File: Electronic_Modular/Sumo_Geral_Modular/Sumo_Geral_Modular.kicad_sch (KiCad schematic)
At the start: 26 parts, among them J1 Conn_01x02, J10 Conn_01x03, J11 Conn_01x03, J2 Conn_01x05, J3 Conn_01x05, J4 Conn_01x05, J5 Conn_01x03, J6 Conn_01x08, J7 Conn_01x08, J8 Conn_01x02, J9 Conn_01x02, SW1 SW_Push, SW2 SW_Push, SW3 SW_Push, U1 AMS1117-5.0, U2 AMS1117-3.3

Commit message: chore: continue development modular pcb
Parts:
- added C7: 100uF, symbol Device:C
- added D2: D, symbol Device:D
- added J12: USB_B_Micro, symbol Connector:USB_B_Micro
- added Q1, Q2: S8050, Package_TO_SOT_THT:TO-92_Inline, symbol Transistor_BJT:S8050
- added R4, R5: 1K, symbol Device:R
- added R6, R7: 10K, symbol Device:R
- added U3: CH340C, Package_SO:SOIC-16_3.9x9.9mm_P1.27mm, symbol Interface_USB:CH340C
- added U4: ESP32-WROOM-32UE, RF_Module:ESP32-WROOM-32UE, symbol RF_Module:ESP32-WROOM-32UE
- J6: value Conn_01x08 -> p H ld e
- J7: value Conn_01x08 -> p H ld d
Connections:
- net 3V3: now also R1.2, R2.2, C7.1, U3.16 (VCC), U3.4 (V3), U4.2 (VDD)
- net 5V: now also D2.1 (K)
- net EN: now also Q1.3 (C), U4.3 (EN)
- net GND: now also C1.2, C2.2, C3.2, C4.2, J1.2 (Pin_2), R3.2, U1.1 (GND), U2.1 (GND), C7.2, J12.5 (GND), J12.6 (Shield), U3.1 (GND), U4.1 (GND), U4.15 (GND), U4.38 (GND), U4.39 (GND); no longer R1.2, R2.2
- net SCL: now also R1.1, U4.36 (IO22); no longer R2.1
- net SDA: now also R2.1, U4.33 (IO21); no longer R1.1
- new net: R5.2, U3.3 (RXD)
- new net: Q2.1 (E), R7.2, U3.14 (~{RTS})
- new net: Q2.2 (B), R7.1
- new net: D2.2 (A), J12.1 (VBUS)
- new net: J12.2 (D-), U3.6 (UD-)
- new net: J12.3 (D+), U3.5 (UD+)
- new net: Q1.1 (E), R6.2, U3.13 (~{DTR})
- new net: Q1.2 (B), R6.1
- new net: R4.2, U3.2 (TXD)
- new net I00: Q2.3 (C)
- new net IO0: U4.25 (IO0)
- new net RXD0: R5.1
- new net TXD0: R4.1
- no-connect marks 5 -> 14
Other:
- moved on the sheet: C1, C2, C3, C4, C5, C6, D1, J1, J10, J11, J2, J3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

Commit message: chore: finish the schematic and set footprints
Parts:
- added D3: LED, symbol Device:LED
- added J13: SENSOR DE MOUSE, Connector_JST:JST_XH_S5B-XH-A_1x05_P2.50mm_Horizontal, symbol Connector_Generic:Conn_01x05
- added J14: ALIMENTAÇÃO SDM, Connector_JST:JST_XH_S2B-XH-A_1x02_P2.50mm_Horizontal, symbol Connector_Generic:Conn_01x02
- added J15: MPU, Connector_PinSocket_2.54mm:PinSocket_1x08_P2.54mm_Vertical, symbol Connector_Generic:Conn_01x08
- added R8: 330, symbol Device:R
- J2: value Conn_01x05 -> VL53L0X 1; footprint (none) -> Connector_JST:JST_XH_B5B-XH-AM_1x05_P2.50mm_Vertical
- J3: value Conn_01x05 -> VL53L0X 2; footprint (none) -> Connector_JST:JST_XH_B5B-XH-AM_1x05_P2.50mm_Vertical
- J4: value Conn_01x05 -> VL53L0X 3; footprint (none) -> Connector_JST:JST_XH_B5B-XH-AM_1x05_P2.50mm_Vertical
- J5: value Conn_01x03 -> VS1838B; footprint (none) -> Connector_PinHeader_2.54mm:PinHeader_1x03_P2.54mm_Vertical
- J6: value p H ld e -> ponte H ld e; footprint (none) -> Connector_PinSocket_2.54mm:PinSocket_1x08_P2.54mm_Vertical
- J7: value p H ld d -> ponte H ld d; footprint (none) -> Connector_PinSocket_2.54mm:PinSocket_1x08_P2.54mm_Vertical
- J8, J9: footprint (none) -> Connector_PinSocket_2.54mm:PinSocket_1x02_P2.54mm_Vertical
- R3: value R -> 1K
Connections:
- net STBY is gone; now on net 3V3: J7.4 (Pin_4)
- net 2s: now also R3.1; no longer D1.2 (A)
- net 3V3: now also J14.1 (Pin_1), J15.1 (Pin_1)
- net AIN1: now also U4.9 (IO33)
- net AIN2: now also U4.10 (IO25)
- net BIN1: now also U4.13 (IO14)
- net BIN2: now also U4.14 (IO12)
- net ESC 1: now also U4.28 (IO17)
- net ESC 2: now also U4.27 (IO16)
- net GND: now also D1.1 (K), D3.1 (K), J14.2 (Pin_2), J15.2 (Pin_2), J15.7 (Pin_7); no longer R3.2
- net IR: now also U4.8 (IO32)
- net RXD0: now also U4.34 (RXD0/IO3)
- net SCL: now also J15.3 (Pin_3)
- net SDA: now also J15.4 (Pin_4)
- net TXD0: now also U4.35 (TXD0/IO1)
- net XSH1: now also U4.6 (IO34)
- net XSH2: now also U4.7 (IO35)
- net XSH3: now also U4.12 (IO27)
- net MOTION: now reaches U4.11 (IO26)
- net MOTION: now also J13.5 (Pin_5)
- net SS/CS: now reaches U4.23 (IO15)
- net SS/CS: now also J13.1 (Pin_1)
- net at U4.24 (IO2): now also R8.1
- net SCLK: now reaches U4.30 (IO18)
- net SCLK: now also J13.3 (Pin_3)
- net MISO: now reaches U4.31 (IO19)
- net MISO: now also J13.2 (Pin_2)
- net MOSI: now reaches U4.37 (IO23)
- net MOSI: now also J13.4 (Pin_4)
- new net: D3.2 (A), R8.2
- new net: D1.2 (A), R3.2
- new net INT: J15.8 (Pin_8)
- no-connect marks 14 -> 18
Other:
- moved on the sheet: C5, C6, C7, D1, D2, J10, J11, J12, J2, J3, J4, J5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

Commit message: chore: set all footprints
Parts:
- C1, C2, C3, C4, C5, C6, C7: footprint (none) -> Capacitor_SMD:C_0201_0603Metric
- D1, D3: footprint (none) -> LED_SMD:LED_0201_0603Metric
- D2: footprint (none) -> Diode_SMD:D_0201_0603Metric
- J1: footprint (none) -> Connector_JST:JST_PH_B2B-PH-K_1x02_P2.00mm_Vertical
- J10, J11: footprint (none) -> Connector_JST:JST_XH_B3B-XH-A_1x03_P2.50mm_Vertical
- J12: footprint (none) -> Connector_USB:USB_Micro-B_Amphenol_10118194_Horizontal
- R1, R2, R3, R4, R5, R6, R7, R8: footprint (none) -> Resistor_SMD:R_0201_0603Metric
- SW1: footprint (none) -> Button_Switch_THT:Nidec_Copal_SH-7010C
- SW2, SW3: footprint (none) -> Button_Switch_SMD:SW_SPST_TL3342
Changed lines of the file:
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@@
 			)
 		)
-		(property "Footprint" ""
+		(property "Footprint" "Connector_JST:JST_PH_B2B-PH-K_1x02_P2.00mm_Vertical"
 			(at 30.48 167.64 0)
 			(effects
@@
 			)
 		)
-		(property "Footprint" ""
+		(property "Footprint" "Capacitor_SMD:C_0201_0603Metric"
 			(at 83.5152 182.88 0)
 			(effects
@@
 			)
 		)
-		(property "Footprint" ""
+		(property "Footprint" "Resistor_SMD:R_0201_0603Metric"
 			(at 206.502 49.53 90)
 			(effects
@@
 			)
 		)
-		(property "Footprint" ""
+		(property "Footprint" "Capacitor_SMD:C_0201_0603Metric"
 			(at 124.1552 182.88 0)
 			(effects
@@
 			)
 		)
-		(property "Footprint" ""
+		(property "Footprint" "Resistor_SMD:R_0201_0603Metric"
 			(at 242.57 130.302 90)
 			(effects
@@
 			)
 		)
-		(property "Footprint" ""
+		(property "Footprint" "Capacitor_SMD:C_0201_0603Metric"
 			(at 96.2152 182.88 0)
 			(effects
@@
 			)
 		)
-		(property "Footprint" ""
+		(property "Footprint" "Capacitor_SMD:C_0201_0603Metric"
 			(at 199.0852 120.65 0)
 			(effects
@@
 			)
 		)
-		(property "Footprint" ""
+		(property "Footprint" "Resistor_SMD:R_0201_0603Metric"
 			(at 176.53 31.242 90)
 			(effects
@@
 			)
 		)
-		(property "Footprint" ""
+		(property "Footprint" "Button_Switch_THT:Nidec_Copal_SH-7010C"
 			(at 48.26 162.56 0)
 			(effects
@@
 			)
 		)
-		(property "Footprint" ""
+		(property "Footprint" "Resistor_SMD:R_0201_0603Metric"
 			(at 52.832 175.26 90)
 			(effects
@@
 			)
 		)
-		(property "Footprint" ""
+		(property "Footprint" "Resistor_SMD:R_0201_0603Metric"
 			(at 212.852 68.58 90)
 			(effects
@@
 			)
 		)
-		(property "Footprint" ""
+		(property "Footprint" "LED_SMD:LED_0201_0603Metric"
 			(at 54.61 184.15 0)
 			(effects
@@
 			)
 		)
-		(property "Footprint" ""
+		(property "Footprint" "Connector_USB:USB_Micro-B_Amphenol_10118194_Horizontal"
 			(at 182.88 138.43 0)
 			(effects
@@
 			)
 		)
-		(property "Footprint" ""
+		(property "Footprint" "Connector_JST:JST_XH_B3B-XH-A_1x03_P2.50mm_Vertical"
 			(at 39.37 127 0)
 			(effects
@@
 			)
 		)
-		(property "Footprint" ""
+		(property "Footprint" "Capacitor_SMD:C_0201_0603Metric"
 			(at 75.8952 73.66 0)
 			(effects
@@
 			)
 		)
-		(property "Footprint" ""
+		(property "Footprint" "Resistor_SMD:R_0201_0603Metric"
 			(at 248.92 141.732 90)
 			(effects
@@
 			)
 		)
-		(property "Footprint" ""
+		(property "Footprint" "LED_SMD:LED_0201_0603Metric"
 			(at 184.15 33.02 0)
 			(effects
@@
 			)
 		)
-		(property "Footprint" ""
+		(property "Footprint" "Diode_SMD:D_0201_0603Metric"
 			(at 193.04 132.08 0)
 			(effects
@@
 			)
 		)
-		(property "Footprint" ""
+		(property "Footprint" "Button_Switch_SMD:SW_SPST_TL3342"
 			(at 19.05 72.39 0)
 			(effects
@@
 			)
 		)
-		(property "Footprint" ""
+		(property "Footprint" "Resistor_SMD:R_0201_0603Metric"
 			(at 247.65 154.432 90)
 			(effects
@@
 			)
 		)
-		(property "Footprint" ""
+		(property "Footprint" "Capacitor_SMD:C_0201_0603Metric"
 			(at 63.1952 182.88 0)
 			(effects
@@
 			)
 		)
-		(property "Footprint" ""
+		(property "Footprint" "Button_Switch_SMD:SW_SPST_TL3342"
 			(at 57.15 72.39 0)
 			(effects
@@
 			)
 		)
-		(property "Footprint" ""
+		(property "Footprint" "Capacitor_SMD:C_0201_0603Metric"
 			(at 37.7952 73.66 0)
 			(effects
@@
 			)
 		)
-		(property "Footprint" ""
+		(property "Footprint" "Connector_JST:JST_XH_B3B-XH-A_1x03_P2.50mm_Vertical"
 			(at 39.37 140.97 0)
 			(effects
@@
 			)
 		)
-		(property "Footprint" ""
+		(property "Footprint" "Resistor_SMD:R_0201_0603Metric"
 			(at 242.57 127.762 90)
 			(effects

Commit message: shore: update PCB
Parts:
- added R9: 10K, Resistor_SMD:R_0201_0603Metric, symbol Device:R
- J1: value Conn_01x02 -> Bateria
- J10: value Conn_01x03 -> ESC1
- J11: value Conn_01x03 -> ESC2
- J8, J9: footprint Connector_PinSocket_2.54mm:PinSocket_1x02_P2.54mm_Vertical -> Connector_JST:JST_XH_B2B-XH-AM_1x02_P2.50mm_Vertical
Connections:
- net 3V3: now also R9.2; no longer C6.1, SW3.1
- net AO1: now also J8.2 (Pin_2); no longer J8.1 (Pin_1)
- net AO2: now also J8.1 (Pin_1); no longer J8.2 (Pin_2)
- net EN: now also C5.2; no longer C5.1
- net GND: now also C5.1; no longer C5.2
- net I00: now also C6.1, SW3.1, R9.1
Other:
- moved on the sheet: C5

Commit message: shore: PCB review
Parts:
- added D4: 1N4007, Diode_SMD:D_0603_1608Metric, symbol Device:D
- added D5: LED, LED_SMD:LED_0603_1608Metric, symbol Device:LED
- added R10: 10K, Capacitor_SMD:C_0603_1608Metric, symbol Device:R
- added R11, R12: 10K, Resistor_SMD:R_0603_1608Metric, symbol Device:R
- added R13: 1K, Resistor_SMD:R_0603_1608Metric, symbol Device:R
- C1, C2, C3, C4, C7: footprint Capacitor_SMD:C_0201_0603Metric -> Capacitor_SMD:C_0603_1608Metric
- C5, C6: value 10uF -> 100nF; footprint Capacitor_SMD:C_0201_0603Metric -> Capacitor_SMD:C_0603_1608Metric
- D1, D3: footprint LED_SMD:LED_0201_0603Metric -> LED_SMD:LED_0603_1608Metric
- D2: value D -> 1N4007; footprint Diode_SMD:D_0201_0603Metric -> Diode_SMD:D_0603_1608Metric
- J13: value SENSOR DE MOUSE -> ADSN-9500
- J14: value ALIMENTAÇÃO SDM -> PS ADSN-9500
- J15: value MPU -> MPU-6050
- J5: footprint Connector_PinHeader_2.54mm:PinHeader_1x03_P2.54mm_Vertical -> Connector_PinHeader_2.00mm:PinHeader_1x03_P2.00mm_Vertical
- J8: value Conn_01x02 -> MA
- J9: value Conn_01x02 -> MB
- Q1, Q2: footprint Package_TO_SOT_THT:TO-92_Inline -> Package_TO_SOT_SMD:SOT-23
- R1, R2, R3, R4, R5, R6, R7, R8: footprint Resistor_SMD:R_0201_0603Metric -> Resistor_SMD:R_0603_1608Metric
- SW1: value SW_Push -> ON/OFF
- SW2: value SW_Push -> EN; footprint Button_Switch_SMD:SW_SPST_TL3342 -> Button_Switch_SMD:SW_SPST_TL3305C
- SW3: value SW_Push -> BOOT; footprint Button_Switch_SMD:SW_SPST_TL3342 -> Button_Switch_SMD:SW_SPST_TL3305C
- U4: footprint RF_Module:ESP32-WROOM-32UE -> RF_Module:ESP32-WROOM-32
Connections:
- net 2s: now also R12.2
- net 3V3: now also R13.1
- net 5V: now also D4.1 (K); no longer C2.1, U1.2 (VO)
- net AIN1: now also U4.13 (IO14); no longer U4.9 (IO33)
- net BIN1: now also U4.11 (IO26); no longer U4.13 (IO14)
- net BIN2: now also U4.12 (IO27); no longer U4.14 (IO12)
- net ESC 1: now also U4.14 (IO12); no longer U4.28 (IO17)
- net ESC 2: now also U4.16 (IO13); no longer U4.27 (IO16)
- net GND: now also D5.1 (K), R11.1
- net INT: now also U4.6 (IO34)
- net IR: now also U4.7 (IO35); no longer U4.8 (IO32)
- net MOTION: now also U4.23 (IO15); no longer U4.11 (IO26)
- net RXD0: now also R4.1; no longer R5.1
- net SS/CS: now also U4.29 (IO5); no longer U4.23 (IO15)
- net TXD0: now also R5.1; no longer R4.1
- net XSH1: now also U4.26 (IO4); no longer U4.6 (IO34)
- net XSH2: now also U4.27 (IO16); no longer U4.7 (IO35)
- net XSH3: now also U4.28 (IO17); no longer U4.12 (IO27)
- net DDT: now reaches U4.5 (SENSOR_VN)
- net DDT: now also R10.1, R11.2
- net at R7.2, U3.14 (~{RTS}): now also Q1.1 (E); no longer Q2.1 (E)
- net at R6.2, U3.13 (~{DTR}): now also Q2.1 (E); no longer Q1.1 (E)
- net AO1: no longer names the net of J6.4 (Pin_4)
- net AO1: now also J8.1 (Pin_1); no longer J8.2 (Pin_2)
- net AO2: no longer names the net of J6.5 (Pin_5)
- net AO2: now also J8.2 (Pin_2); no longer J8.1 (Pin_1)
- net BO1: no longer names the net of J6.7 (Pin_7), J9.2 (Pin_2)
- net BO2: no longer names the net of J6.6 (Pin_6), J9.1 (Pin_1)
- new net: C2.1, D4.2 (A), U1.2 (VO)
- new net: R10.2, R12.1
- new net: D5.2 (A), R13.2
- no-connect marks 18 -> 19
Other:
- moved on the sheet: J10, J11, J8, J9, R8

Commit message: shore: schematic final review
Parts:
- added C8: C_Polarized, Capacitor_SMD:C_0603_1608Metric, symbol Device:C_Polarized
- added R14: 10K, Resistor_SMD:R_0603_1608Metric, symbol Device:R
- R9: footprint Resistor_SMD:R_0201_0603Metric -> Resistor_SMD:R_0603_1608Metric
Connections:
- net 3V3: now also R14.1
- net EN: now also C8.1, R14.2
- net GND: now also C8.2
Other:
- moved on the sheet: J10, J11, R10, R11, R12

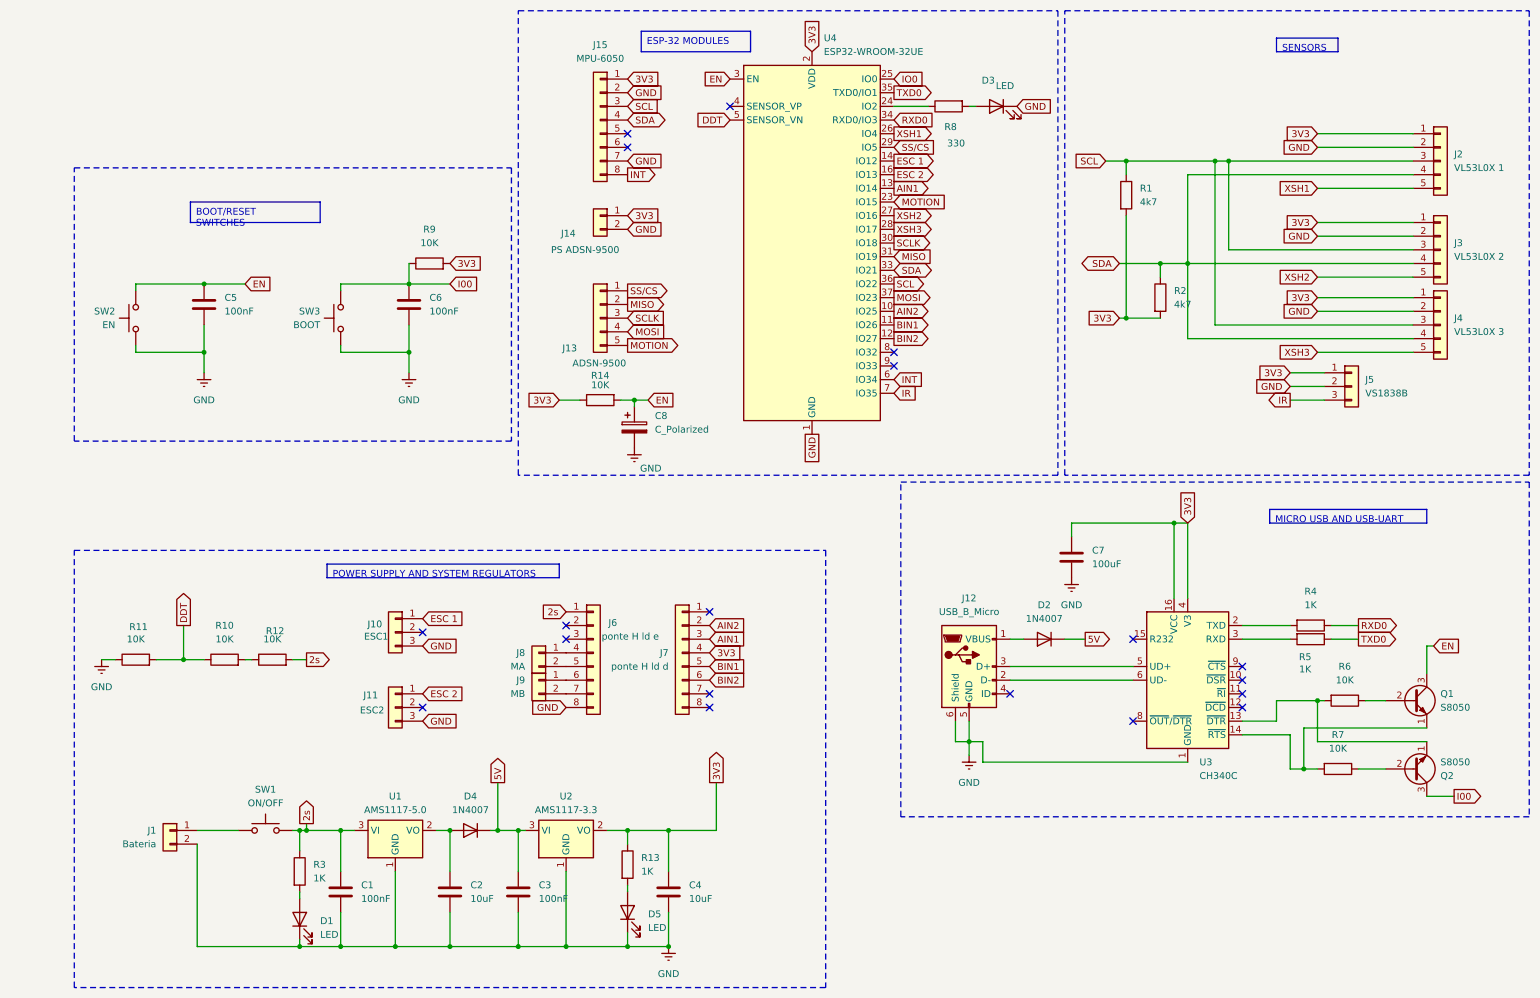
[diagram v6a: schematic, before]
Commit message: chore(Electronics): new symbols and footprints
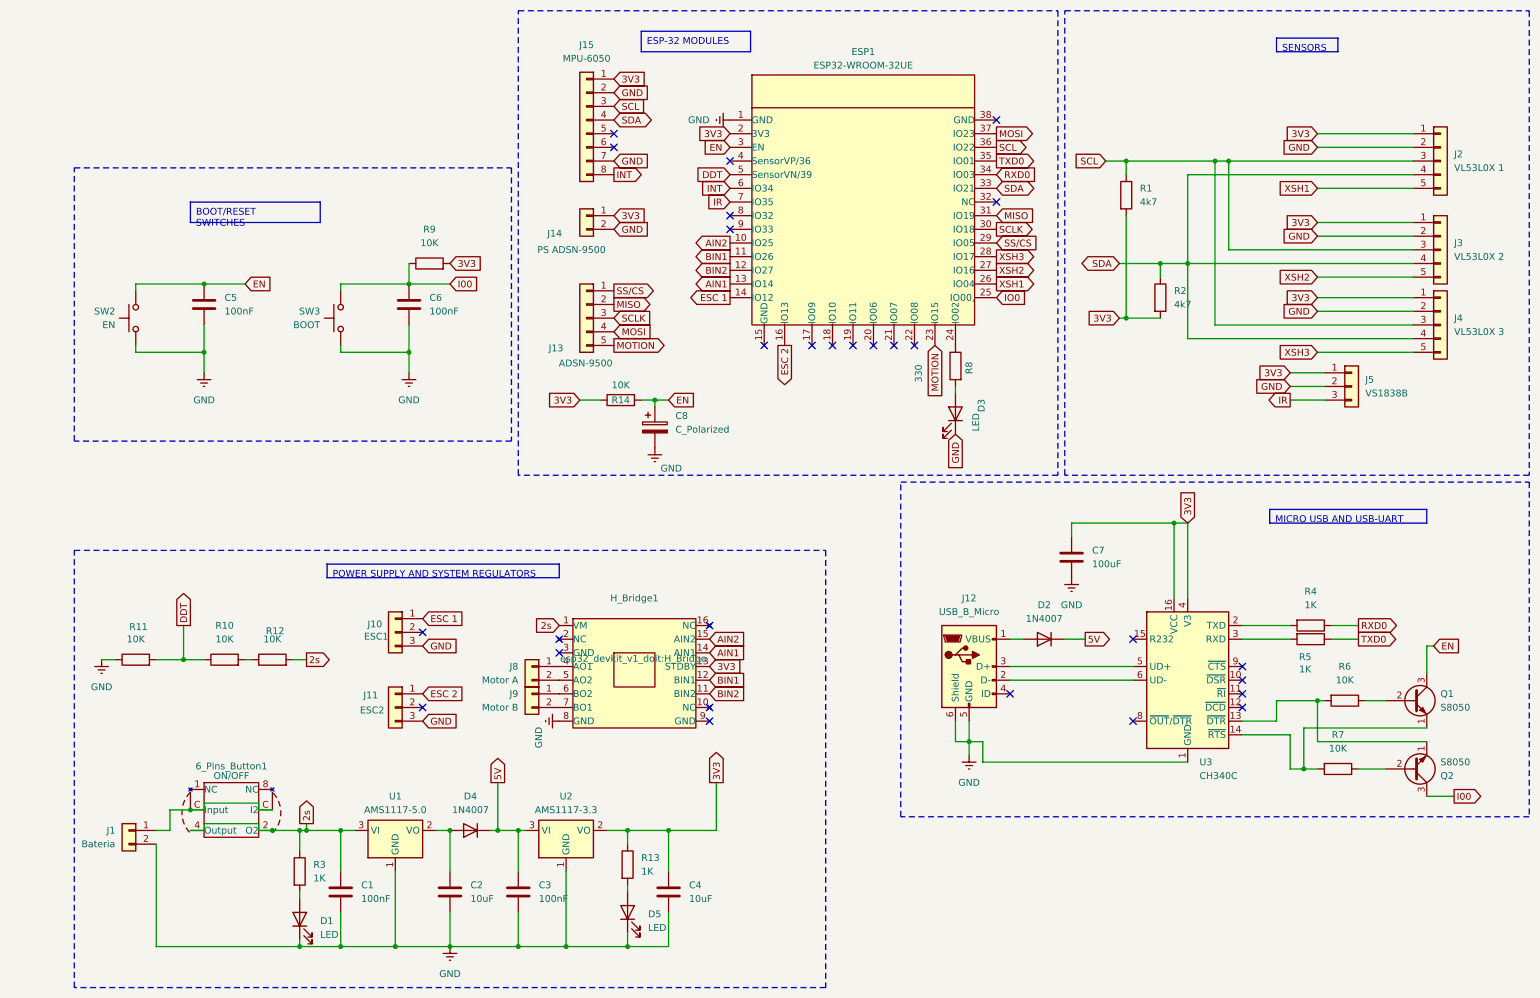
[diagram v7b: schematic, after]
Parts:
- removed J6: ponte H ld e, Connector_PinSocket_2.54mm:PinSocket_1x08_P2.54mm_Vertical, symbol Connector_Generic:Conn_01x08
- removed J7: ponte H ld d, Connector_PinSocket_2.54mm:PinSocket_1x08_P2.54mm_Vertical, symbol Connector_Generic:Conn_01x08
- removed SW1: ON/OFF, Button_Switch_THT:Nidec_Copal_SH-7010C, symbol Switch:SW_Push
- removed U4: ESP32-WROOM-32UE, RF_Module:ESP32-WROOM-32, symbol RF_Module:ESP32-WROOM-32UE
- added 6_Pins_Button1: ON/OFF, Button_Switch_THT:Nidec_Copal_SH-7010C, symbol esp32_devkit_v1_doit:Button_6_Pins
- added ESP1: ESP32-WROOM­32UE, RF_Module:ESP32-WROOM-32, symbol esp32_devkit_v1_doit:ESP32-WROOM­32UE
- added H_Bridge1: ~, esp32_devkit_v1_doit:H_Bridge, symbol esp32_devkit_v1_doit:H_Bridge
- J8: value MA -> Motor A
- J9: value MB -> Motor B
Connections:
- net 2s: now also 6_Pins_Button1.2 (O2), 6_Pins_Button1.4 (Output), H_Bridge1.1 (VM)
- net 3V3: now also ESP1.2 (3V3), H_Bridge1.13 (STDBY)
- net AIN1: now also ESP1.13 (IO14), H_Bridge1.14 (AIN1)
- net AIN2: now also ESP1.10 (IO25), H_Bridge1.15 (AIN2)
- net BIN1: now also ESP1.11 (IO26), H_Bridge1.12 (BIN1)
- net BIN2: now also ESP1.12 (IO27), H_Bridge1.11 (BIN2)
- net DDT: now also ESP1.5 (SensorVN/39)
- net EN: now also ESP1.3 (EN)
- net ESC 1: now also ESP1.14 (IO12)
- net ESC 2: now also ESP1.16 (IO13)
- net GND: now also ESP1.1 (GND), H_Bridge1.8 (GND)
- net INT: now also ESP1.6 (IO34)
- net IO0: now also ESP1.25 (IO00,)
- net IR: now also ESP1.7 (IO35)
- net MISO: now also ESP1.31 (IO19)
- net MOSI: now also ESP1.37 (IO23)
- net MOTION: now also ESP1.23 (IO15)
- net RXD0: now also ESP1.34 (IO03)
- net SCL: now also ESP1.36 (IO22)
- net SCLK: now also ESP1.30 (IO18)
- net SDA: now also ESP1.33 (IO21)
- net SS/CS: now also ESP1.29 (IO05)
- net TXD0: now also ESP1.35 (IO01)
- net XSH1: now also ESP1.26 (IO04)
- net XSH2: now also ESP1.27 (IO16)
- net XSH3: now also ESP1.28 (IO17)
- net at J1.1 (Pin_1): now also 6_Pins_Button1.C (Input)
- net at R8.1: now also ESP1.24 (IO02)
- net at J9.1 (Pin_1): now also H_Bridge1.6 (BO2)
- net at J9.2 (Pin_2): now also H_Bridge1.7 (BO1)
- net at J8.1 (Pin_1): now also H_Bridge1.4 (AO1)
- net at J8.2 (Pin_2): now also H_Bridge1.5 (AO2)
- no-connect marks 19 -> 28
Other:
- moved on the sheet: C8, J1, J13, J14, J15, R14
